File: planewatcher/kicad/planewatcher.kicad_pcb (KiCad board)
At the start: 4 copper layers, 86.1 x 54 mm, 170 parts, among them J1 Conn_01x02, J2 RF_IN, J3 BMI-S-209-F, J4 FPGA BANK 33, J5 FPGA BANK 35 V1.2/V1.3, Q1 DMP6023LSS-13, U1 LT8608MSE, U10 AD8138ARZ, U11 AD9203ARUZ, U12 LT8640IUDCF-1#PBF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

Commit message: MOAR VIAS
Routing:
- net GND: vias 531 -> 535

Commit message: work on silk screening
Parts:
- moved TP11 0.43 mm to (30.7, 18.7)
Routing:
- net GND: vias 535 -> 542
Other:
- board text added: "+"
- board text added: "-"
- board text added: "1"
- board text added: "12V IN"
- board text added: "2"
- board text added: "3"
- board text added: "4"
- board text added: "JP1: FPGA PWR ON:5V OFF:NC"
- board text added: "RF IN"
- board text added: "plane watcher"
- board text added: "rev: 0.0"

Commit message: work on silkscreen & vias under regulators
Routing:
- net GND: vias 542 -> 626
- net /Power_3V_Analog/VIN: vias 4 -> 5
- added copper zone on F.Cu, net /Power_Input/IN

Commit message: minor updates while reviewing
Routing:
- net GND: vias 626 -> 717

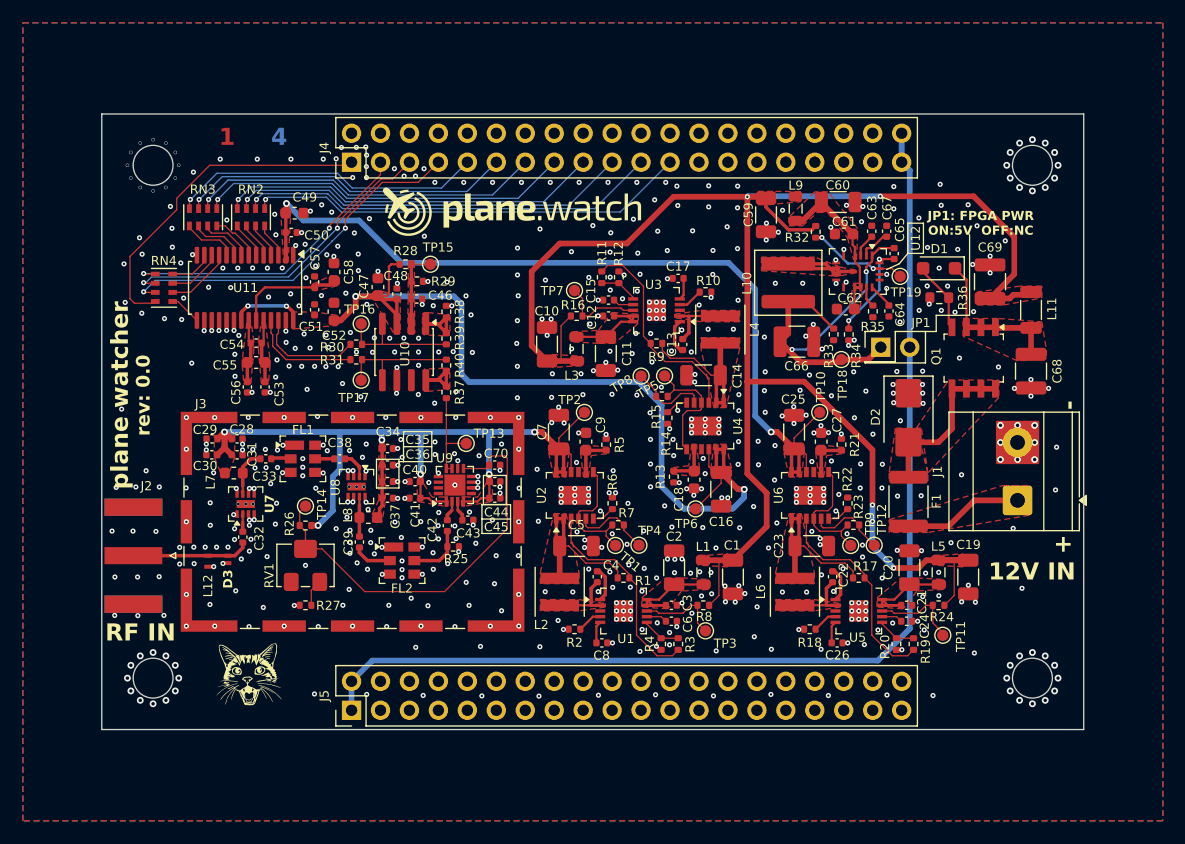
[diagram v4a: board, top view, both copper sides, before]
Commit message: add jumpers for testing different power rails & additional test point
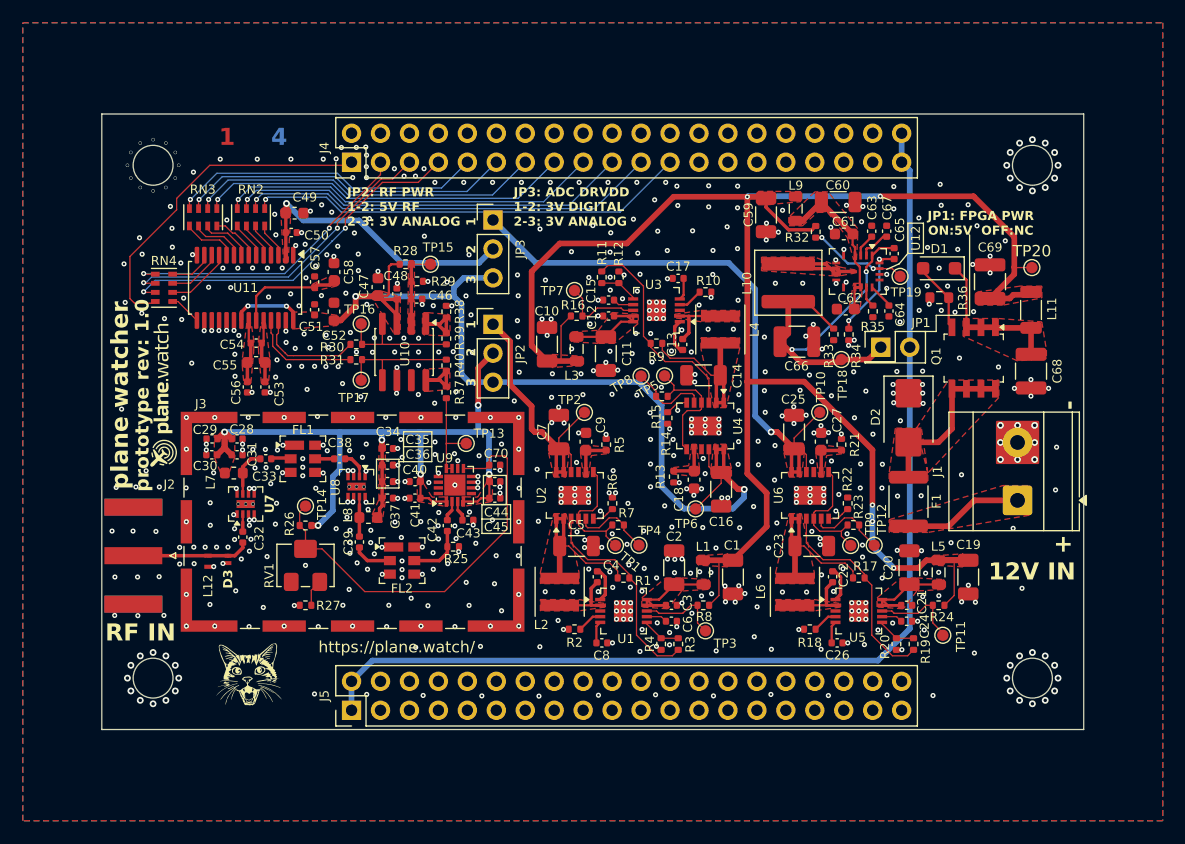
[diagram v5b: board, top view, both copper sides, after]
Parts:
- added JP2: RF Power Select, Connector_PinHeader_2.54mm:PinHeader_1x03_P2.54mm_Vertical, F.Cu at (-8.75, -8.55)
- added JP3: RF Power Select, Connector_PinHeader_2.54mm:PinHeader_1x03_P2.54mm_Vertical, F.Cu at (-8.75, -17.7)
- added TP20: V+, TestPoint:TestPoint_Pad_D1.0mm, F.Cu at (38.5, -13.5)
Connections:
- C28 pad 2: 5V_RF -> /LNA_Stage_1/VIN
- C29 pad 1: 5V_RF -> /LNA_Stage_1/VIN
- C30 pad 1: 5V_RF -> /LNA_Stage_1/VIN
- C31 pad 2: 5V_RF -> /LNA_Stage_1/VIN
- C34 pad 2: 5V_RF -> /LNA_Stage_1/VIN
- C35 pad 1: 5V_RF -> /LNA_Stage_1/VIN
- C36 pad 1: 5V_RF -> /LNA_Stage_1/VIN
- C37 pad 2: 5V_RF -> /LNA_Stage_1/VIN
- C40 pad 2: 5V_RF -> /LNA_Stage_1/VIN
- C41 pad 2: 5V_RF -> /LNA_Stage_1/VIN
- C44 pad 2: 5V_RF -> /LNA_Stage_1/VIN
- C45 pad 2: 5V_RF -> /LNA_Stage_1/VIN
- C49 pad 1: DRVDD -> /ADC/DRVDD
- C50 pad 1: DRVDD -> /ADC/DRVDD
- L7 pad 1: 5V_RF -> /LNA_Stage_1/VIN
- L8 pad 1: 5V_RF -> /LNA_Stage_1/VIN
- R26 pad 1: 5V_RF -> /LNA_Stage_1/VIN
- U11 pad 2: DRVDD -> /ADC/DRVDD
- U9 pad 1: 5V_RF -> /LNA_Stage_1/VIN
- U9 pad 4: 5V_RF -> /LNA_Stage_1/VIN
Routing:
- net /LNA_Stage_1/VIN: track 0.00 -> 70.5 mm, vias 0 -> 6
- net 5V_RF: track 81.9 -> 25.6 mm, vias 6 -> 0
- net /ADC/DRVDD: track 0.00 -> 25.4 mm, vias 0 -> 1
- net DRVDD: track 76.5 -> 53.2 mm, vias 2 -> 1
- net AVDD: track 88.5 -> 93.1 mm
- net /Power_3V_Analog/VIN: track 162.9 -> 164.5 mm
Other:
- board text added: "JP2: RF PWR 1-2: 5V RF 2-3: 3V ANALOG"
- board text added: "JP3: ADC DRVDD 1-2: 3V DIGITAL 2-3: 3V ANALOG"
- board text added: "https://plane.watch/"
- board text added: "prototype rev: 1.0"
- board text removed: "rev: 0.0"

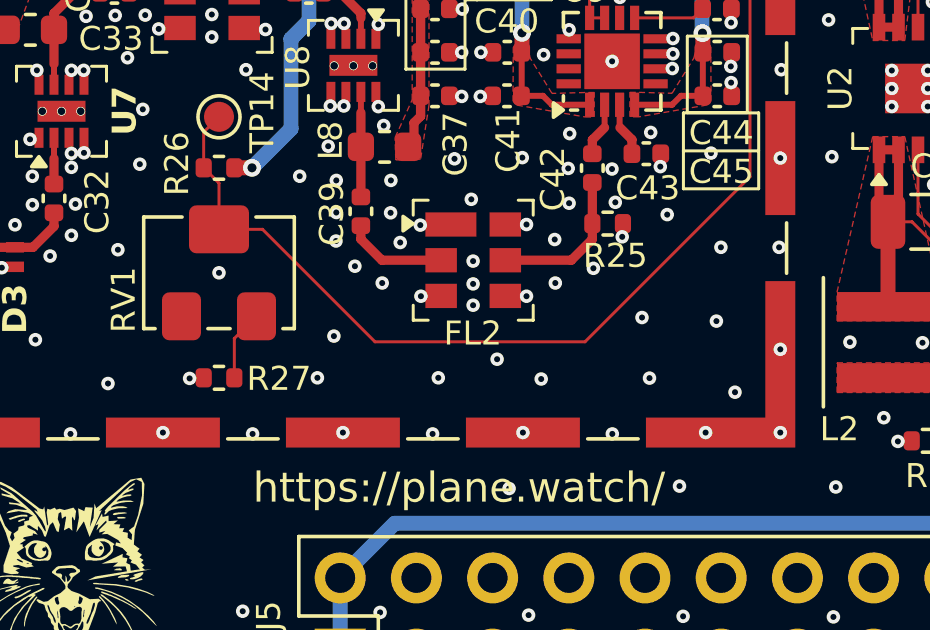
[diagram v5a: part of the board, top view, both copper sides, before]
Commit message: address & fix ERC errors/warnings
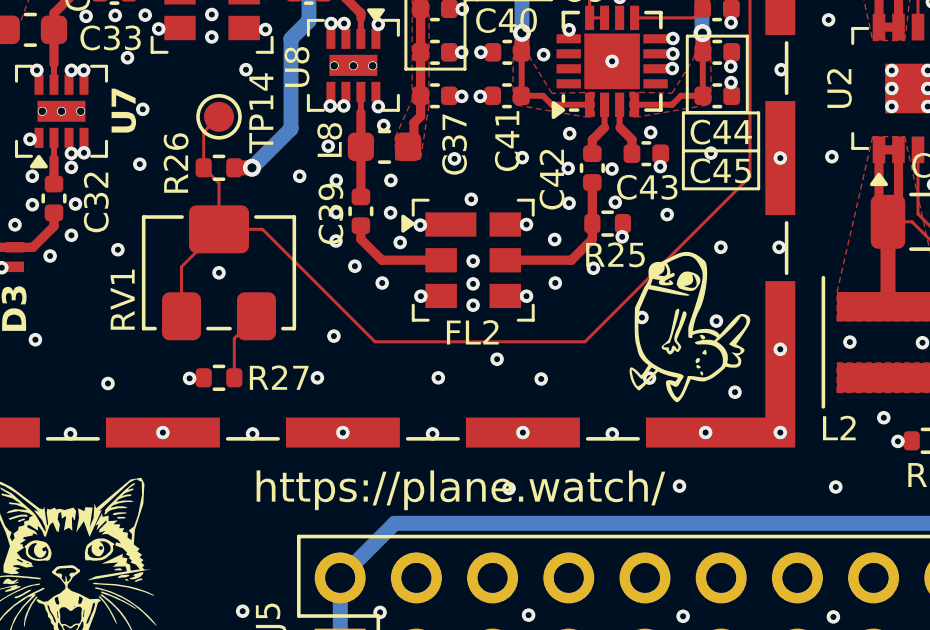
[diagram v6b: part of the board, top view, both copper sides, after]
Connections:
- RV1 pad 1: unconnected-(RV1-Pad1) -> Net-(U9-TADJ)
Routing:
- net Net-(U9-TADJ): track 37.4 -> 40.8 mm
